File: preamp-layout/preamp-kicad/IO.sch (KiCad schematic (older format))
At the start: 20 parts, among them J10 Conn_Coaxial_x2, J11 Conn_01x03_Female, J12 Conn_01x03_Female, J13 Conn_01x03_Female, J14 Conn_01x03_Female, J15 Conn_01x03_Female, J16 XLR3, J17 XLR3, J18 Conn_01x03_Female, J19 Conn_01x03_Female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

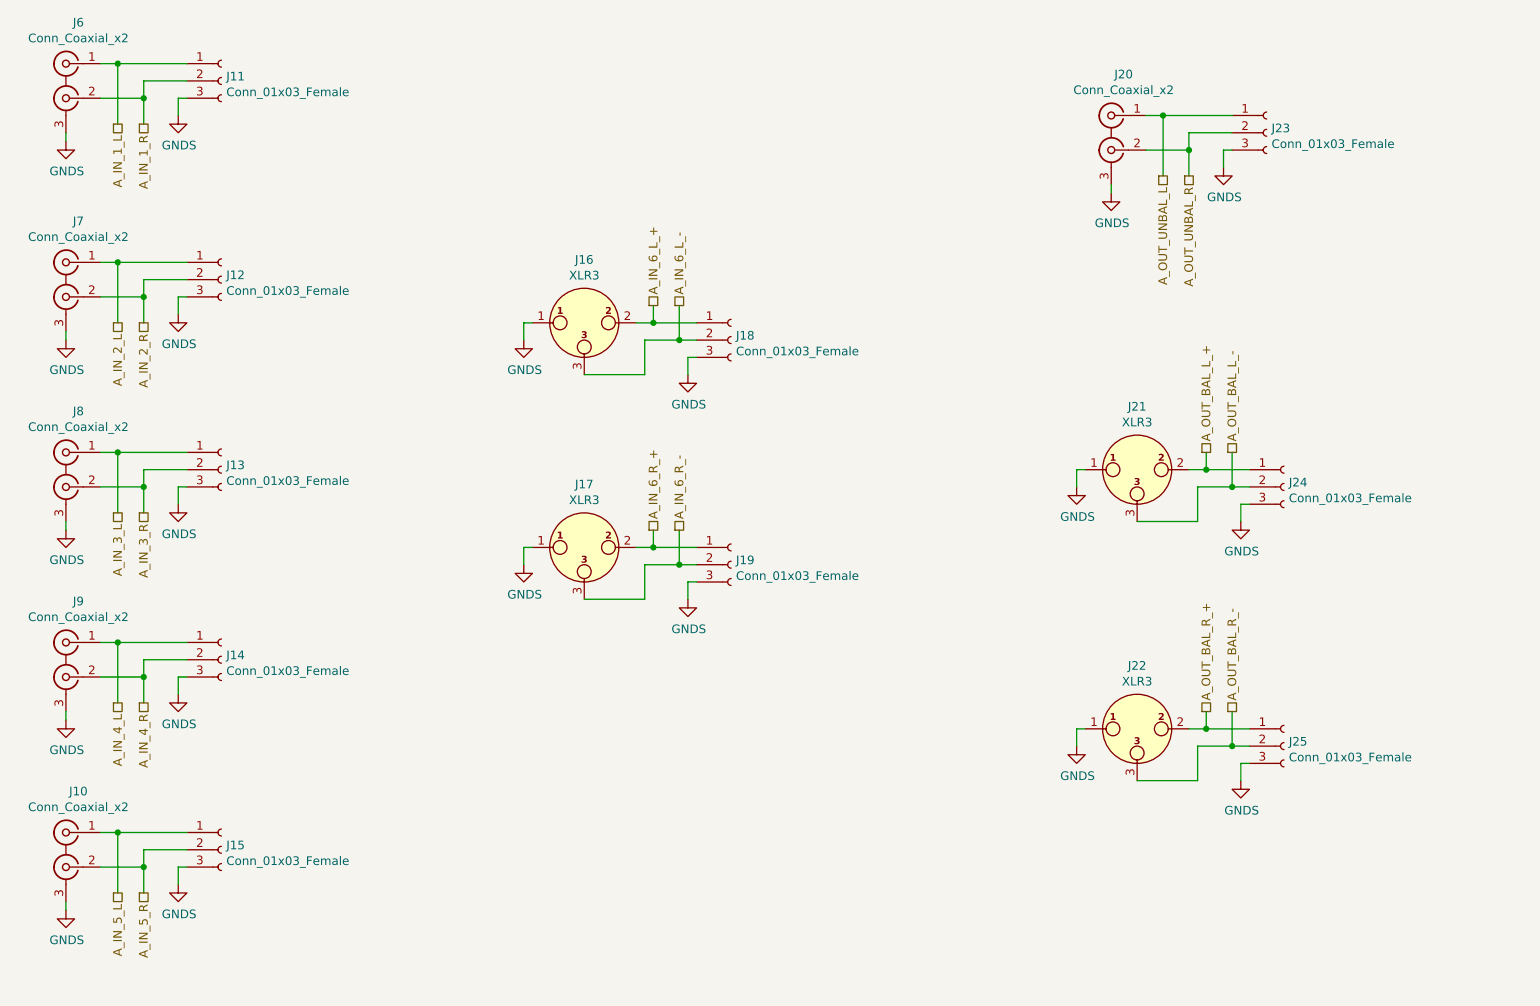
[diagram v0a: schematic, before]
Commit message: BOM skeleton added. gitignore updated to ignore schematic bak files. General work done on the schematic layout.
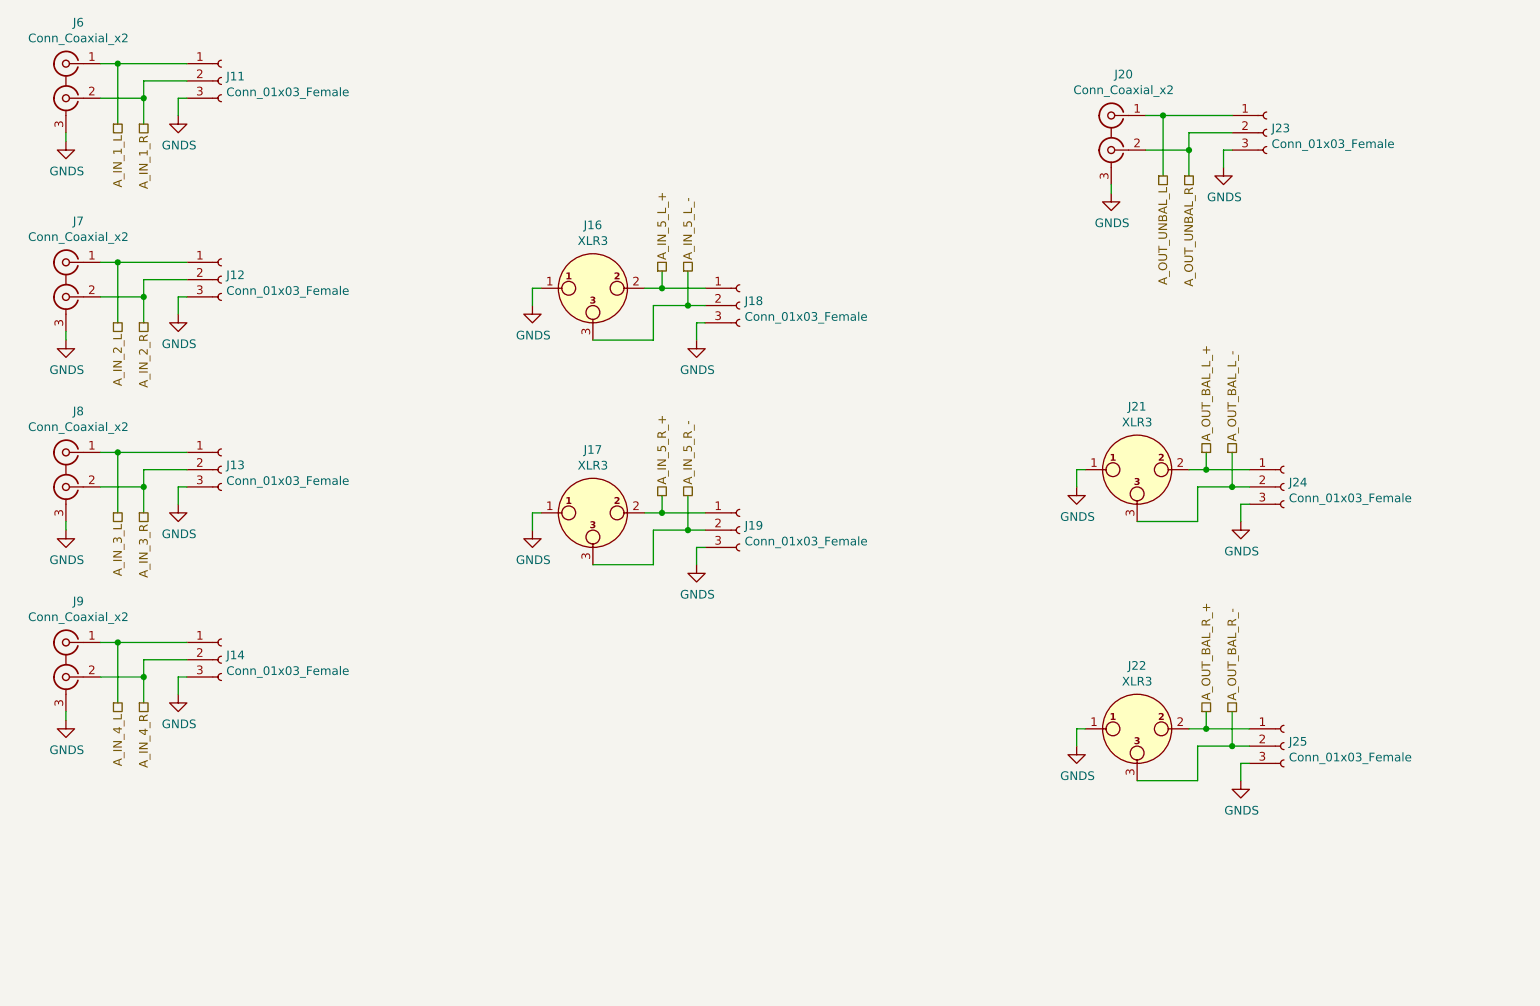
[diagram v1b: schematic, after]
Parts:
- removed J10: Conn_Coaxial_x2, symbol Connector:Conn_Coaxial_x2
- removed J15: Conn_01x03_Female, symbol Connector:Conn_01x03_Female
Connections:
- net A_IN_6_L_+ renamed A_IN_5_L_+
- net A_IN_6_L_- renamed A_IN_5_L_-
- net A_IN_6_R_+ renamed A_IN_5_R_+
- net A_IN_6_R_- renamed A_IN_5_R_-
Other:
- moved on the sheet: J16, J17, J18, J19

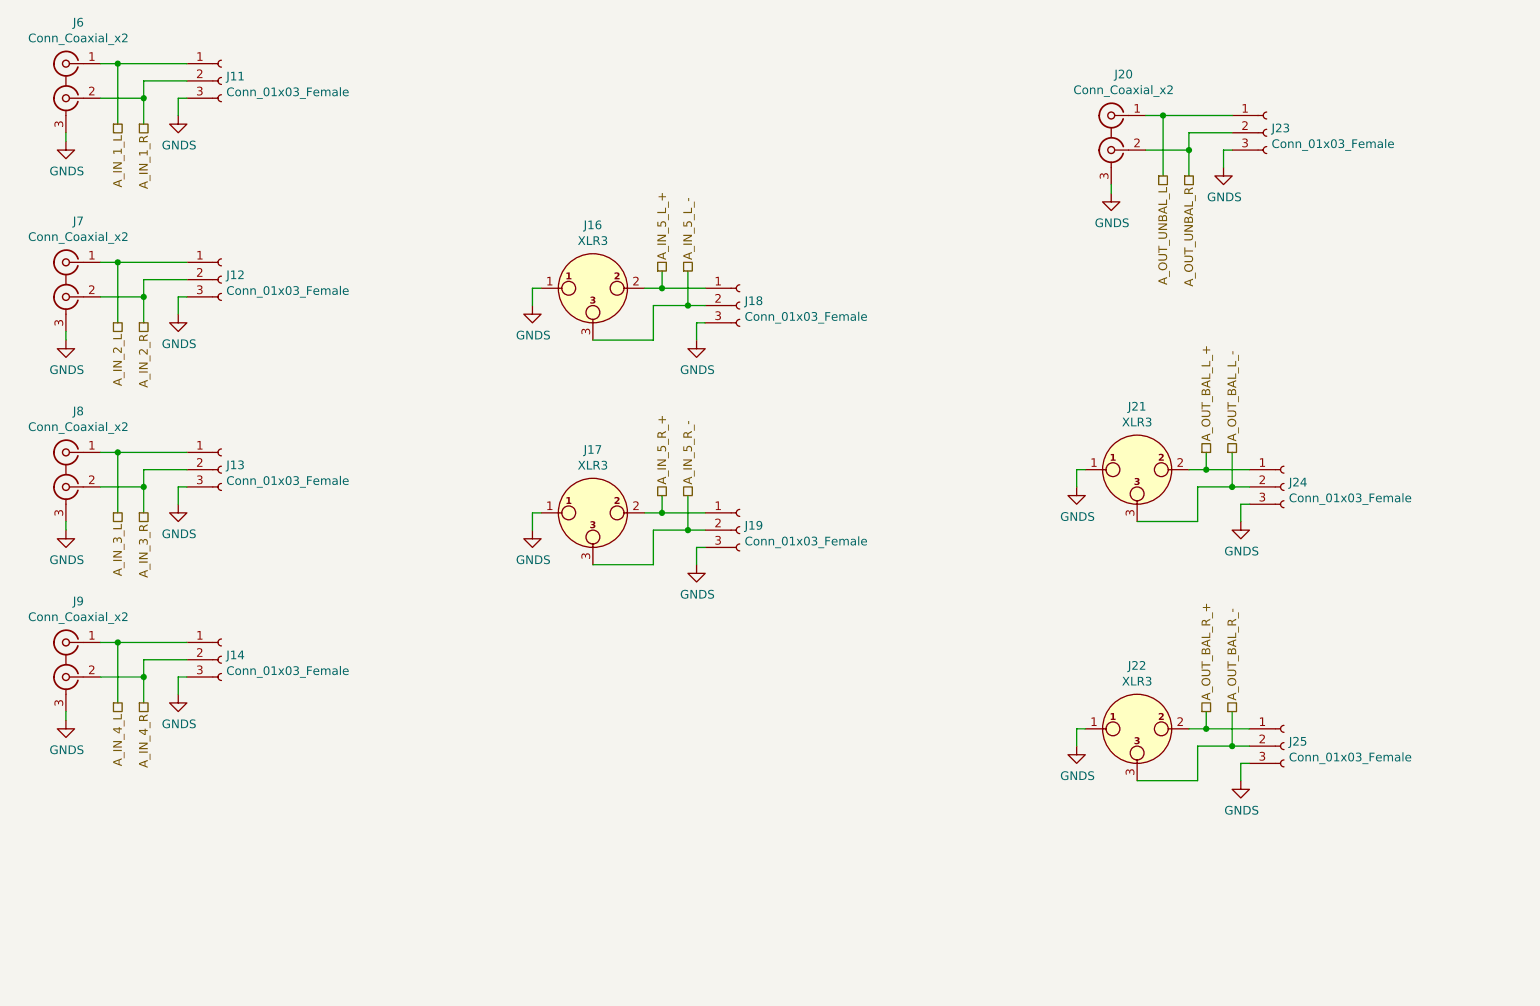
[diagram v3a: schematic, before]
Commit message: IO layout cleanup
Changed location of bal/unbal buffers from selector board to daughter board. Generalized IO PCB to accept daughter boards, not specific to connector type or bal/unbal. The idea is that as many unbalanced RCAs can be populated on the main IO board as desired and jumper cables can also be added to daughter boards as needed for different kinds of IO, but the interface to the selector board does not need to change to allow this.
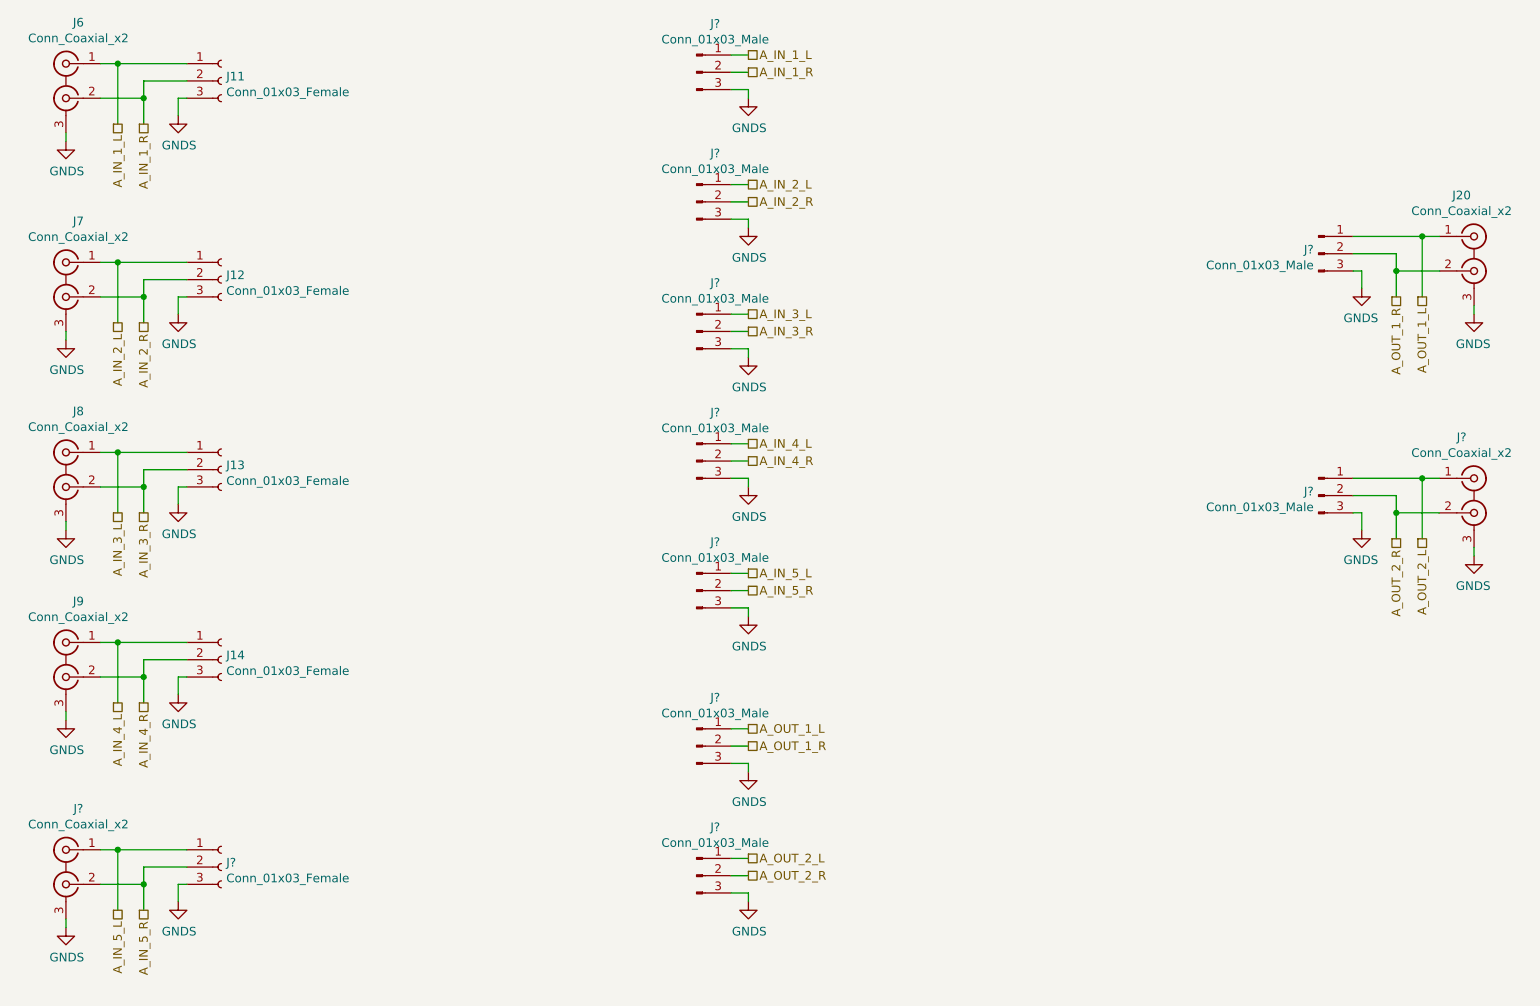
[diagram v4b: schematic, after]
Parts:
- removed J16, J17, J21, J22: XLR3, symbol Connector:XLR3
- removed J18, J19, J23, J24, J25: Conn_01x03_Female, symbol Connector:Conn_01x03_Female
- added J? (x2): Conn_Coaxial_x2, symbol Connector:Conn_Coaxial_x2
- added J?: Conn_01x03_Female, symbol Connector:Conn_01x03_Female
- added J? (x9): Conn_01x03_Male, symbol Connector:Conn_01x03_Male
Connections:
- net A_IN_1_L: now also J?.1 (Pin_1)
- net A_IN_1_R: now also J?.2 (Pin_2)
- net A_IN_2_L: now also J?.1 (Pin_1)
- net A_IN_2_R: now also J?.2 (Pin_2)
- net A_IN_3_L: now also J?.1 (Pin_1)
- net A_IN_3_R: now also J?.2 (Pin_2)
- net A_IN_4_L: now also J?.1 (Pin_1)
- net A_IN_4_R: now also J?.2 (Pin_2)
- net GNDS: now also J?.3 (EXT), J?.3 (EXT), J?.3 (Pin_3), J?.3 (Pin_3), J?.3 (Pin_3), J?.3 (Pin_3), J?.3 (Pin_3), J?.3 (Pin_3), J?.3 (Pin_3), J?.3 (Pin_3), J?.3 (Pin_3), J?.3 (Pin_3)
- net A_OUT_UNBAL_L renamed A_OUT_1_L
- net A_OUT_1_L: now also J?.1 (Pin_1), J?.1 (Pin_1)
- net A_OUT_UNBAL_R renamed A_OUT_1_R
- net A_OUT_1_R: now also J?.2 (Pin_2), J?.2 (Pin_2)
- new net A_IN_5_L: J?.1 (IN1), J?.1 (Pin_1), J?.1 (Pin_1)
- new net A_IN_5_R: J?.2 (IN2), J?.2 (Pin_2), J?.2 (Pin_2)
- new net A_OUT_2_L: J?.1 (IN1), J?.1 (Pin_1), J?.1 (Pin_1)
- new net A_OUT_2_R: J?.2 (IN2), J?.2 (Pin_2), J?.2 (Pin_2)
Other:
- moved on the sheet: J20
